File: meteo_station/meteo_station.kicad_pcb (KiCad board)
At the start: 2 copper layers, 100 x 100 mm, 16 parts, among them SW1 SW_SPDT, U1 TP4056, U2 ESP32-WROOM, U3 DS18B20, U4 BH1750, U5 BME280

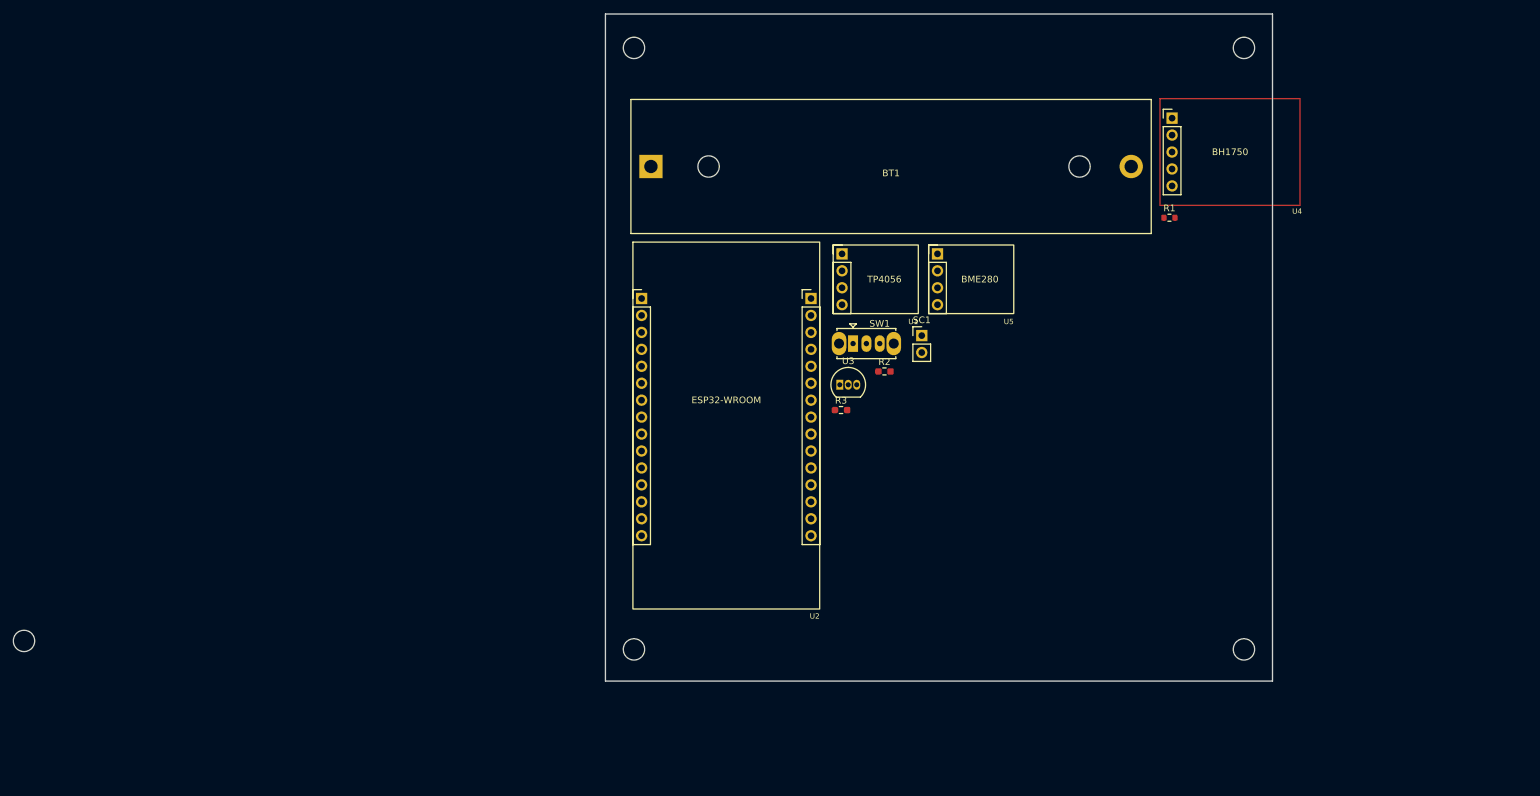
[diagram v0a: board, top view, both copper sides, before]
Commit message: Add some footprints
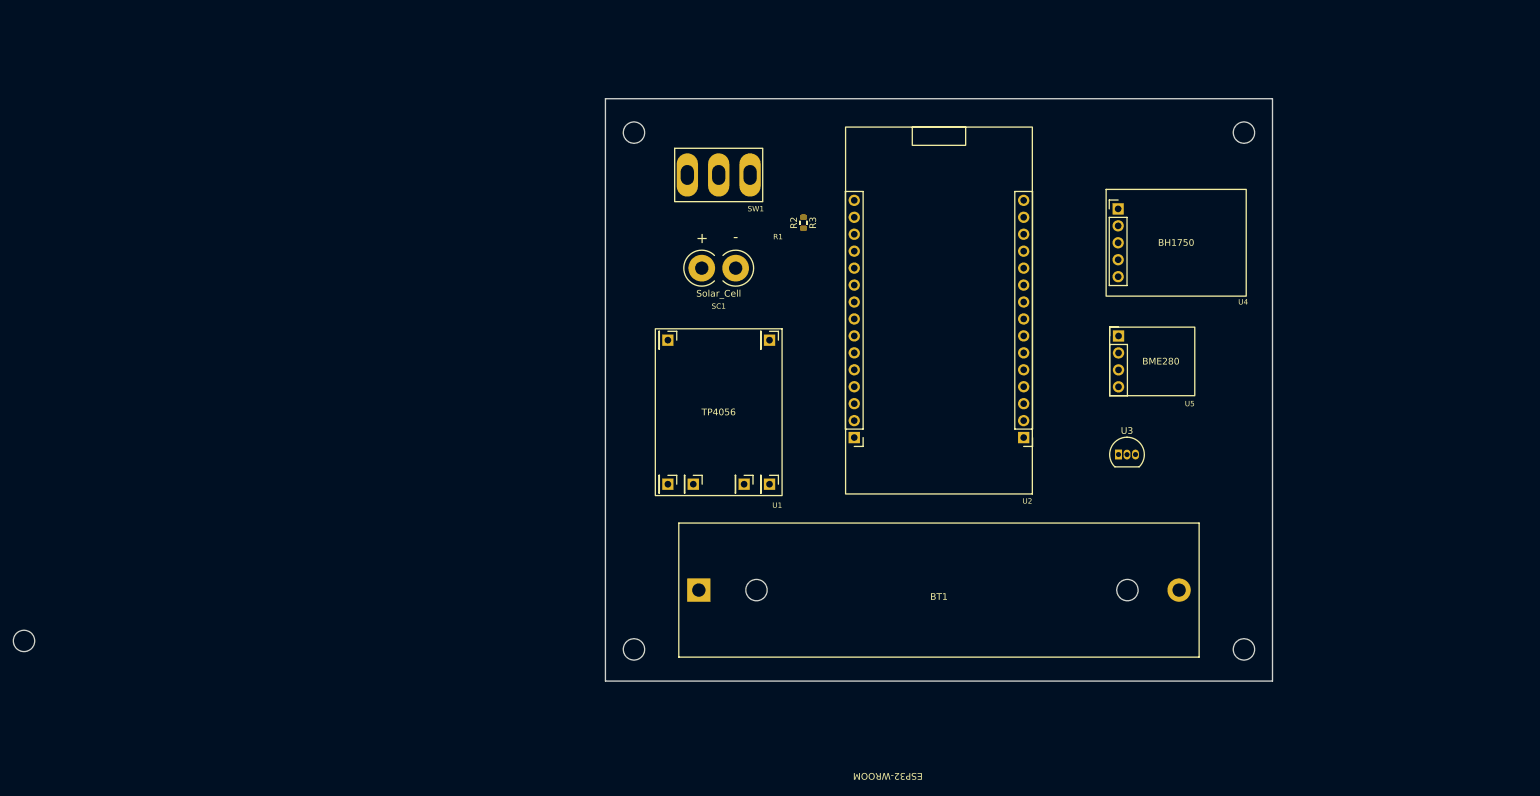
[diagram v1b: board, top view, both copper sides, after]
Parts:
- R2, R3: footprint Resistor_SMD:R_0603_1608Metric_Pad0.98x0.95mm_HandSolder -> Resistor_SMD:R_0603_1608Metric
- SC1: footprint Connector_PinHeader_2.54mm:PinHeader_1x02_P2.54mm_Vertical -> meteo_station_footprints:SolarPanel
- SW1: footprint Button_Switch_THT:SW_Slide_1P2T_CK_OS102011MS2Q -> meteo_station_footprints:MTS102
- U1: footprint meteo_station_footprints:BME280 -> meteo_station_footprints:TP4056
- moved BT1 63.9 mm to (113.9, 137.2)
- moved R1 54.9 mm to (129.5, 82.1), turned to 90 degrees
- moved U3 43.1 mm to (176.8, 116.8)
- moved U2 36.2 mm to (149.9, 95.2), turned to 180 degrees
- moved SW1 32.3 mm to (116.8, 74.9)
- moved SC1 32.1 mm to (116.8, 88.9), turned to 90 degrees
- moved U5 29.8 mm to (176.8, 102.9)
- moved R3 28.6 mm to (129.5, 82.1), turned to -90 degrees
- moved U1 27.2 mm to (116.8, 110.5), turned to -90 degrees
- moved R2 25.4 mm to (129.5, 82.1), turned to 90 degrees
- moved U4 15.8 mm to (185.4, 85.1)
- moved REF** 12.7 mm to (104.1, 68.6)
- moved REF** 12.7 mm to (195.6, 68.6)
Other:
- board size 100 x 100 mm -> 100 x 87.3 mm

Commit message: Preliminary design
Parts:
- moved R2 43.6 mm to (168.9, 100.8)
- moved R1 41.5 mm to (168.9, 95.2)
- moved U3 14.2 mm to (191.0, 116.8)
- moved U4 14.1 mm to (183.3, 99.1)
- moved U5 14.1 mm to (174.7, 116.8)
- moved R3 1.27 mm to (130.8, 82.1)
- moved SC1 1.27 mm to (116.8, 87.6), turned to -90 degrees
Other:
- board text added: "alicja.space"
- board text added: "meteo station"
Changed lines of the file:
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@@
   (net 35 "unconnected-(U2-Pad27)")
   (footprint "meteo_station_footprints:BH1750" (layer "F.Cu")
-    (at 185.42 85.09)
+    (at 183.35 99.06)
     (property "Sheetfile" "meteo_station.kicad_sch")
     (property "Sheetname" "")
@@
   )
   (footprint "Resistor_SMD:R_0603_1608Metric" (layer "F.Cu")
-    (at 129.54 82.105 90)
+    (at 168.91 100.775 90)
     (descr "Resistor SMD 0603 (1608 Metric), square (rectangular) end terminal, IPC_7351 nominal, (Body size source: IPC-SM-782 page 72, https://www.pcb-3d.com/wordpress/wp-content/uploads/ipc-sm-782a_amendment_1_and_2.pdf), generated with kicad-footprint-generator")
     (tags "resistor")
@@
     (property "Sheetname" "")
     (attr smd)
-    (fp_text reference "R2" (at 0 -1.43 90) (layer "F.SilkS")
-      (effects (font (size 1 1) (thickness 0.15)))
+    (fp_text reference "R2" (at -2.27 0 180) (layer "F.SilkS")
+      (effects (font (size 0.8 0.8) (thickness 0.15)))
     )
     (fp_text value "4.7K" (at 0 1.43 90) (layer "F.Fab")
@@
   )
   (footprint "meteo_station_footprints:SolarPanel" (layer "F.Cu")
-    (at 116.84 88.9 90)
+    (at 116.84 87.63 -90)
     (property "Sheetfile" "meteo_station.kicad_sch")
     (property "Sheetname" "")
     (attr through_hole)
-    (fp_text reference "SC1" (at -5.715 0 unlocked) (layer "F.SilkS")
+    (fp_text reference "SC1" (at 3.81 0 unlocked) (layer "F.SilkS")
       (effects (font (size 0.8 0.8) (thickness 0.15)))
     )
-    (fp_text value "Solar_Cell" (at -3.81 0 unlocked) (layer "F.SilkS")
-      (effects (font (size 1 1) (thickness 0.15)))
-    )
-    (fp_text user "+" (at 4.445 -2.54 90 unlocked) (layer "F.SilkS")
+    (fp_text value "Solar_Cell" (at 5.715 0 unlocked) (layer "F.SilkS")
+      (effects (font (size 1 1) (thickness 0.15)))
+    )
+    (fp_text user "+" (at -4.01 -2.54 -90 unlocked) (layer "F.SilkS")
       (effects (font (size 1.6 1.6) (thickness 0.4)))
     )
-    (fp_text user "-" (at 4.445 2.539999 180 unlocked) (layer "F.SilkS")
+    (fp_text user "-" (at -4.01 2.539999 unlocked) (layer "F.SilkS")
       (effects (font (size 1.6 1.6) (thickness 0.4)))
     )
-    (fp_text user "${REFERENCE}" (at 0 6.985 90 unlocked) (layer "F.Fab")
+    (fp_text user "${REFERENCE}" (at 0 6.985 -90 unlocked) (layer "F.Fab")
       (effects (font (size 1 1) (thickness 0.15)))
     )
     (fp_arc (start 1.904998 0.635) (mid -0.000001 5.234074) (end -1.905 0.635) (layer "F.SilkS") (width 0.2))
     (fp_arc (start -1.904999 -0.635001) (mid 0 -5.234075) (end 1.904999 -0.635001) (layer "F.SilkS") (width 0.2))
-    (pad "1" thru_hole custom (at 0 -2.54 90) (size 4 4) (drill 2) (layers *.Cu *.Mask)
+    (pad "1" thru_hole custom (at 0 -2.54 270) (size 4 4) (drill 2) (layers *.Cu *.Mask)
       (net 7 "Net-(SC1-Pad1)") (pinfunction "+") (pintype "passive")
       (options (clearance outline) (anchor circle))
       (primitives
       ))
-    (pad "2" thru_hole custom (at 0 2.54 90) (size 4 4) (drill 2) (layers *.Cu *.Mask)
+    (pad "2" thru_hole custom (at 0 2.54 270) (size 4 4) (drill 2) (layers *.Cu *.Mask)
       (net 8 "Net-(SC1-Pad2)") (pinfunction "-") (pintype "passive")
       (options (clearance outline) (anchor circle))
@@
       (effects (font (size 0.8 0.8) (thickness 0.15)) (justify right))
     )
-    (fp_text value "ESP32-WROOM" (at 7.66 -69.8 180 unlocked) (layer "F.SilkS")
-      (effects (font (size 1 1) (thickness 0.15)))
-    )
-    (fp_text user "${REFERENCE}" (at 7.66 -91.39 180 unlocked) (layer "F.Fab")
+    (fp_text value "ESP32-WROOM" (at 0 0 unlocked) (layer "F.SilkS")
+      (effects (font (size 1 1) (thickness 0.15)))
+    )
+    (fp_text user "${REFERENCE}" (at 0 -2.54 unlocked) (layer "F.Fab")
       (effects (font (size 1 1) (thickness 0.15)))
     )
@@
   )
   (footprint "meteo_station_footprints:BME280" (layer "F.Cu")
-    (at 176.7775 102.88)
+    (at 174.7075 116.85)
     (property "Sheetfile" "meteo_station.kicad_sch")
     (property "Sheetname" "")
@@
   )
   (footprint "Resistor_SMD:R_0603_1608Metric" (layer "F.Cu")
-    (at 129.54 82.105 90)
+    (at 168.91 95.25 90)
     (descr "Resistor SMD 0603 (1608 Metric), square (rectangular) end terminal, IPC_7351 nominal, (Body size source: IPC-SM-782 page 72, https://www.pcb-3d.com/wordpress/wp-content/uploads/ipc-sm-782a_amendment_1_and_2.pdf), generated with kicad-footprint-generator")
     (tags "resistor")
@@
     (property "Sheetname" "")
     (attr smd)
-    (fp_text reference "R1" (at -2.095 -3.81 180) (layer "F.SilkS")
+    (fp_text reference "R1" (at -2.27 0 180) (layer "F.SilkS")
       (effects (font (size 0.8 0.8) (thickness 0.15)))
     )
@@
   )
   (footprint "Package_TO_SOT_THT:TO-92_Inline" (layer "F.Cu")
-    (at 176.7775 116.84)
+    (at 190.97 116.84)
     (descr "TO-92 leads in-line, narrow, oval pads, drill 0.75mm (see NXP sot054_po.pdf)")
     (tags "to-92 sc-43 sc-43a sot54 PA33 transistor")
@@
     (property "Sheetname" "")
     (attr through_hole)
-    (fp_text reference "U3" (at 1.27 -3.56) (layer "F.SilkS")
-      (effects (font (size 1 1) (thickness 0.15)))
+    (fp_text reference "U3" (at 1.27 2.81) (layer "F.SilkS")
+      (effects (font (size 0.8 0.8) (thickness 0.15)))
     )
     (fp_text value "DS18B20" (at 1.27 2.79) (layer "F.Fab")
@@
   )
   (footprint "Resistor_SMD:R_0603_1608Metric" (layer "F.Cu")
-    (at 129.54 82.105 -90)
+    (at 130.81 82.105 -90)
     (descr "Resistor SMD 0603 (1608 Metric), square (rectangular) end terminal, IPC_7351 nominal, (Body size source: IPC-SM-782 page 72, https://www.pcb-3d.com/wordpress/wp-content/uploads/ipc-sm-782a_amendment_1_and_2.pdf), generated with kicad-footprint-generator")
     (tags "resistor")
@@
     (property "Sheetname" "")
     (attr smd)
-    (fp_text reference "R3" (at 0 -1.43 -90) (layer "F.SilkS")
-      (effects (font (size 1 1) (thickness 0.15)))
+    (fp_text reference "R3" (at 2.27 0) (layer "F.SilkS")
+      (effects (font (size 0.8 0.8) (thickness 0.15)))
     )
     (fp_text value "4.7K" (at 0 1.43 -90) (layer "F.Fab")
@@
   )
   (gr_rect (start 99.86 63.5) (end 199.86 150.8) (layer "Edge.Cuts") (width 0.2) (fill none))
+  (gr_text "alicja.space" (at 189.23 80.01) (layer "F.SilkS")
+    (effects (font (size 1 1) (thickness 0.15)))
+  )
+  (gr_text "meteo station" (at 182.88 77.47) (layer "F.SilkS")
+    (effects (font (size 2.2 2.2) (thickness 0.15)))
+  )
   (dimension (type aligned) (layer "Dwgs.User")
-    (pts (xy 149.86 62.23) (xy 199.86 62.23))
-    (height 124.46)
-    (gr_text "50.0000 mm" (at 174.86 185.54) (layer "Dwgs.User")
+    (pts (xy 97.79 112.23) (xy 97.79 162.23))
+    (height -136.36)
+    (gr_text "50.0000 mm" (at 233 137.23 90) (layer "Dwgs.User")
       (effects (font (size 1 1) (thickness 0.15)))
     )
@@
   )
   (dimension (type aligned) (layer "Dwgs.User")
-    (pts (xy 99.86 112.23) (xy 99.86 162.23))
-    (height -136.36)
-    (gr_text "50.0000 mm" (at 235.07 137.23 90) (layer "Dwgs.User")
-      (effects (font (size 1 1) (thickness 0.15)))
-    )
+    (pts (xy 199.86 76.645) (xy 149.86 76.645))
+    (height -114.3)
+    (gr_text "50.0000 mm" (at 174.86 189.795) (layer "Dwgs.User")
+      (effects (font (size 1 1) (thickness 0.15)))
+    )

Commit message: Add some routes
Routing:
- net GND: track 0.00 -> 143.1 mm
- net 3V3: track 0.00 -> 116.9 mm
- net Net-(R3-Pad2): track 0.00 -> 109.5 mm
- net SCL: track 0.00 -> 87.4 mm
- net Net-(BT1-Pad2): track 0.00 -> 84.2 mm
- net SDA: track 0.00 -> 76.5 mm
- net Net-(SW1-Pad1): track 0.00 -> 59.7 mm
- net Net-(SW1-Pad2): track 0.00 -> 54.8 mm, vias 0 -> 1
- net Net-(BT1-Pad1): track 0.00 -> 18.7 mm
- net Net-(SC1-Pad2): track 0.00 -> 14.2 mm
- net Net-(SC1-Pad1): track 0.00 -> 14.2 mm
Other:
- board text added: "lorem ipsum"
- board text removed: "meteo station"

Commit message: PCB adjustments
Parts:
- removed the REF** at (104.1, 68.6)
- removed the REF** at (104.1, 146.1)
- removed the REF** at (195.6, 68.6)
- removed the REF** at (195.6, 146.1)
- removed the REF** at (12.7, 144.8)
- added C1: 100nF, Capacitor_SMD:C_0603_1608Metric, F.Cu at (222.2, 78.7)
- added C2: 100nF, Capacitor_SMD:C_0603_1608Metric, F.Cu at (234.2, 68.9)
- added C3: 2.2uF, Capacitor_Tantalum_SMD:CP_EIA-3216-18_Kemet-A, F.Cu at (223.1, 75.9)
- added D1: D_Schottky, Diode_SMD:D_SMB_Handsoldering, F.Cu at (229.5, 64.9)
- added D2: D_Schottky, Diode_SMD:D_SMB_Handsoldering, F.Cu at (215.0, 77.1)
- added R4: 4.7K, Resistor_SMD:R_0603_1608Metric, F.Cu at (236.7, 63.3)
- added R5: 4.7K, Resistor_SMD:R_0603_1608Metric, F.Cu at (236.7, 65.8)
- added REF**: MountingHole_3.2mm_M3, MountingHole:MountingHole_3.2mm_M3, F.Cu at (199.9, 146.0)
- added REF**: MountingHole_3.2mm_M3, MountingHole:MountingHole_3.2mm_M3, F.Cu at (99.9, 146.0)
- added REF**: MountingHole_3.2mm_M3, MountingHole:MountingHole_3.2mm_M3, F.Cu at (199.9, 66.0)
- added REF**: MountingHole_3.2mm_M3, MountingHole:MountingHole_3.2mm_M3, F.Cu at (99.9, 66.0)
- added SC2: Solar_Cell, meteo_station_footprints:SolarPanel_JST, F.Cu at (228.2, 71.0)
- added U6: BME280, meteo_station_footprints:BME280, F.Cu at (181.6, 115.6)
- BT1: footprint Battery:BatteryHolder_MPD_BH-18650-PC2 -> meteo_station_footprints:BatteryHolder
- R1, R2: value 4.7K -> 10K
- SC1: footprint meteo_station_footprints:SolarPanel -> meteo_station_footprints:SolarPanel_JST
- U2: value ESP32-WROOM -> LF33_TO220; footprint meteo_station_footprints:ESP32-WROOM -> Package_TO_SOT_THT:TO-220-3_Vertical
- U3: value DS18B20 -> ESP32-WROOM; footprint Package_TO_SOT_THT:TO-92_Inline -> meteo_station_footprints:ESP32-WROOM
- U4: value BH1750 -> DS18B20; footprint meteo_station_footprints:BH1750 -> meteo_station_footprints:TO-92_Inline
- U5: value BME280 -> BH1750; footprint meteo_station_footprints:BME280 -> meteo_station_footprints:BH1750
- moved U3 47.7 mm to (149.9, 92.7)
- moved U2 44.0 mm to (106.0, 90.8)
- moved BT1 36.0 mm to (149.9, 137.2)
- moved U4 23.8 mm to (199.1, 116.8), turned to 90 degrees
- moved U5 23.6 mm to (184.2, 95.2)
- moved R1 2.54 mm to (168.9, 92.7)
- moved R2 2.54 mm to (168.9, 98.2)
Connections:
- R1 pad 1: 3V3 -> BAT_V
- R1 pad 2: SCL -> OUT+
- R2 pad 1: 3V3 -> BAT_V
- R2 pad 2: SDA -> OUT-
- R3 pad 2: Net-(R3-Pad2) -> SCL
- SC1 pad 1: Net-(SC1-Pad1) -> Net-(D1-Pad2)
- SW1 pad 1: Net-(SW1-Pad1) -> OUT+
- U1 pad 1: Net-(SC1-Pad1) -> Net-(D1-Pad1)
- U1 pad 6: GND -> OUT-
- U2 pad 1: unconnected-(U2-Pad1) -> OUT+
- U2 pad 2: unconnected-(U2-Pad2) -> OUT-
- U2 pad 3: unconnected-(U2-Pad3) -> 3V3
- U3 pad 1: GND -> unconnected-(U3-Pad1)
- U3 pad 2: Net-(R3-Pad2) -> unconnected-(U3-Pad2)
- U3 pad 3: 3V3 -> unconnected-(U3-Pad3)
- U4 pad 1: 3V3 -> OUT-
- U4 pad 2: GND -> Net-(R5-Pad2)
- U4 pad 3: SCL -> 3V3
- U5 pad 2: GND -> OUT-
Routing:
- net GND: track 143.1 -> 0.00 mm
- net 3V3: track 116.9 -> 0.00 mm
- net Net-(R3-Pad2): track 109.5 -> 0.00 mm
- net SCL: track 87.4 -> 0.00 mm
- net Net-(BT1-Pad2): track 84.2 -> 0.00 mm
- net SDA: track 76.5 -> 0.00 mm
- net Net-(SW1-Pad1): track 59.7 -> 0.00 mm
- net Net-(SW1-Pad2): track 54.8 -> 0.00 mm, vias 1 -> 0
- net Net-(BT1-Pad1): track 18.7 -> 0.00 mm
- net Net-(SC1-Pad2): track 14.2 -> 0.00 mm
- net Net-(SC1-Pad1): track 14.2 -> 0.00 mm
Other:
- board size 100 x 87.3 mm -> 110 x 90 mm

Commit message: PCB v2
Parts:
- D1, D2: footprint Diode_SMD:D_SMB_Handsoldering -> Diode_SMD:D_SMB
- U2: footprint Package_TO_SOT_THT:TO-220-3_Vertical -> Package_TO_SOT_THT:TO-220-3_Horizontal_TabDown
- moved C2 140.4 mm to (102.2, 116.8)
- moved C3 129.3 mm to (102.2, 121.9)
- moved D1 117.4 mm to (113.0, 79.4), turned to 180 degrees
- moved SC2 102.8 mm to (125.5, 70.5)
- moved C1 92.4 mm to (132.7, 101.6), turned to 90 degrees
- moved D2 89.6 mm to (125.5, 79.4), turned to 180 degrees
- moved R5 78.3 mm to (167.0, 101.6), turned to 90 degrees
- moved R4 76.8 mm to (167.0, 95.7), turned to -90 degrees
- moved R3 37.1 mm to (167.0, 90.2)
- moved R1 36.3 mm to (132.7, 90.2)
- moved R2 36.3 mm to (132.7, 95.7)
- moved SW1 28.2 mm to (102.2, 99.1), turned to 90 degrees
- moved U2 26.3 mm to (109.5, 116.8), turned to -90 degrees
- moved SC1 17.6 mm to (113.0, 70.5), turned to 0 degrees
- moved U1 12.3 mm to (119.4, 98.4)
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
